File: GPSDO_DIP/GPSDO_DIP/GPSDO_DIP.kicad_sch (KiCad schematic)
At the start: 86 parts, among them IC2 74HC14, K1 Conn_01x04, K2 Conn_Coaxial, K3 Conn_01x02, K4 Jumper_3_Open, K5 Conn_01x02, K9 Conn_Coaxial, U1 Pico, U10 U1, U11 74HC14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

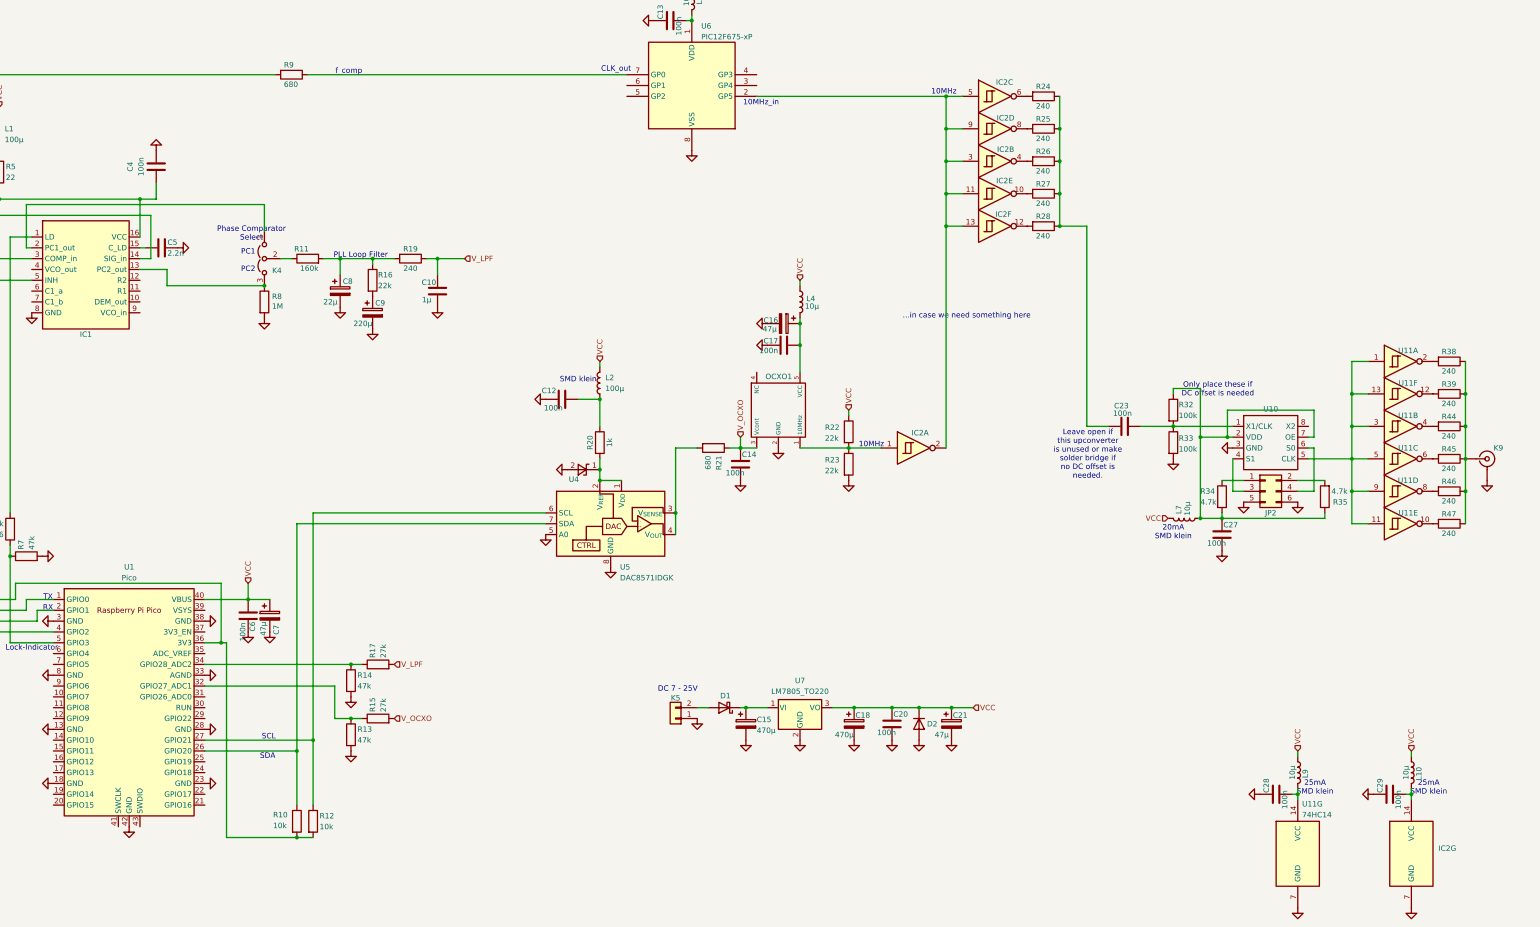
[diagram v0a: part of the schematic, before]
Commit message: added mounting holes & 10MHz SMA-port, cleaned up labels a bit
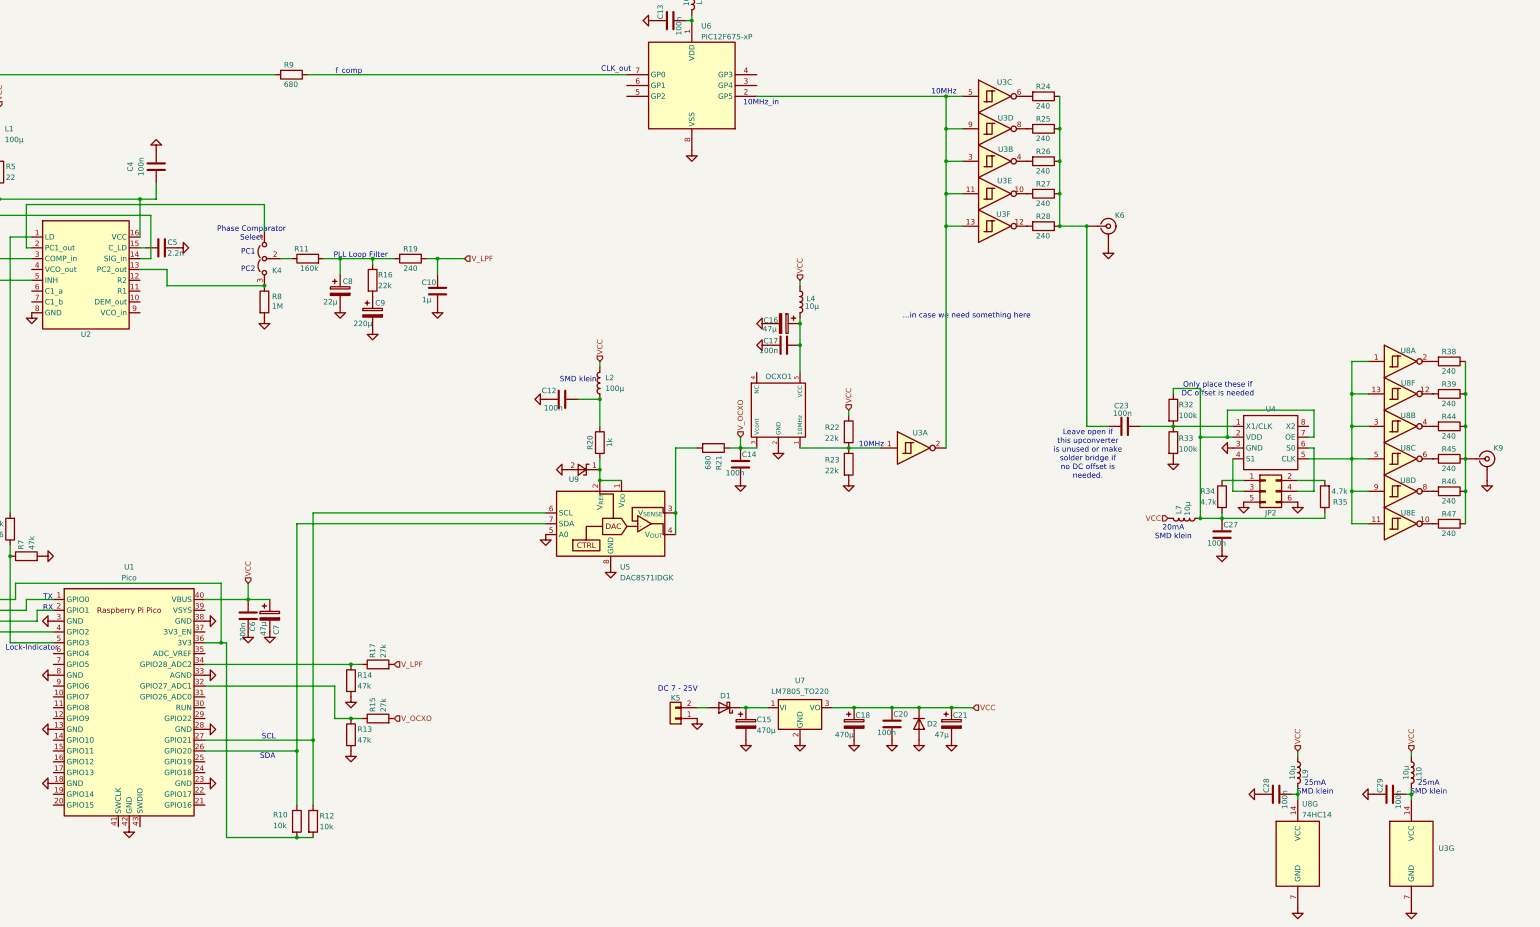
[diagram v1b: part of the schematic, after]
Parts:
- added K6: Conn_Coaxial, Connector_Coaxial:SMA_Molex_73251-1153_EdgeMount_Horizontal, symbol Connector:Conn_Coaxial
- renumbered IC1 to U2, IC2 to U3, U10 to U4, U11 to U8, U4 to U9
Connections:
- net GND: now also K6.2 (Ext)
- net at C23.2, R24.1, R25.1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: now also K6.1 (In)
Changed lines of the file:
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@@
 	)
 	(junction
+		(at 307.34 87.63)
+		(diameter 0)
+		(color 0 0 0 0)
+	)
+	(junction
 		(at 383.54 220.98)
 		(diameter 0)
@@
 		(on_board yes)
 		(dnp no)
-		(property "Reference" "IC2"
+		(property "Reference" "U3"
 			(at 288.036 53.848 0)
 			(effects
@@
 			(project "GPSDO_DIP"
 				(path "/39e4adc2-ce33-4fe2-95cd-1c444a71fa67"
-					(reference "IC2")
+					(reference "U3")
 					(unit 3)
 				)
@@
 	)
 	(symbol
+		(lib_id "power:GND")
+		(at 312.42 92.71 0)
+		(unit 1)
+		(exclude_from_sim no)
+		(in_bom yes)
+		(on_board yes)
+		(dnp no)
+		(fields_autoplaced yes)
+		(property "Reference" "#PWR022"
+			(at 312.42 99.06 0)
+			(effects
+				(font
+					(size 1.27 1.27)
+				)
+				(hide yes)
+			)
+		)
+		(property "Value" "GND"
+			(at 312.42 97.79 0)
+			(effects
+				(font
+					(size 1.27 1.27)
+				)
+				(hide yes)
+			)
+		)
+		(property "Footprint" ""
+			(at 312.42 92.71 0)
+			(effects
+				(font
+					(size 1.27 1.27)
+				)
+				(hide yes)
+			)
+		)
+		(property "Datasheet" ""
+			(at 312.42 92.71 0)
+			(effects
+				(font
+					(size 1.27 1.27)
+				)
+				(hide yes)
+			)
+		)
+		(property "Description" "Power symbol creates a global label with name \"GND\" , ground"
+			(at 312.42 92.71 0)
+			(effects
+				(font
+					(size 1.27 1.27)
+				)
+				(hide yes)
+			)
+		)
+		(pin "1"
+		)
+		(instances
+			(project "GPSDO_DIP"
+				(path "/39e4adc2-ce33-4fe2-95cd-1c444a71fa67"
+					(reference "#PWR022")
+					(unit 1)
+				)
+			)
+		)
+	)
+	(symbol
 		(lib_id "Device:R")
 		(at 140.97 190.5 90)
@@
 		(dnp no)
 		(fields_autoplaced yes)
-		(property "Reference" "IC2"
+		(property "Reference" "U3"
 			(at 389.89 233.6799 0)
 			(effects
@@
 			(project "GPSDO_DIP"
 				(path "/39e4adc2-ce33-4fe2-95cd-1c444a71fa67"
-					(reference "IC2")
+					(reference "U3")
 					(unit 7)
 				)
@@
 		(on_board yes)
 		(dnp no)
-		(property "Reference" "IC2"
+		(property "Reference" "U3"
 			(at 288.29 62.23 0)
 			(effects
@@
 			(project "GPSDO_DIP"
 				(path "/39e4adc2-ce33-4fe2-95cd-1c444a71fa67"
-					(reference "IC2")
+					(reference "U3")
 					(unit 4)
 				)
@@
 		(on_board yes)
 		(dnp no)
-		(property "Reference" "U11"
+		(property "Reference" "U8"
 			(at 382.778 147.32 0)
 			(effects
@@
 			(project "GPSDO_DIP"
 				(path "/39e4adc2-ce33-4fe2-95cd-1c444a71fa67"
-					(reference "U11")
+					(reference "U8")
 					(unit 4)
 				)
@@
 		(on_board yes)
 		(dnp no)
-		(property "Reference" "U11"
+		(property "Reference" "U8"
 			(at 382.778 154.94 0)
 			(effects
@@
 			(project "GPSDO_DIP"
 				(path "/39e4adc2-ce33-4fe2-95cd-1c444a71fa67"
-					(reference "U11")
+					(reference "U8")
 					(unit 5)
 				)
@@
 		(on_board yes)
 		(dnp no)
-		(property "Reference" "IC2"
+		(property "Reference" "U3"
 			(at 288.036 76.962 0)
 			(effects
@@
 			(project "GPSDO_DIP"
 				(path "/39e4adc2-ce33-4fe2-95cd-1c444a71fa67"
-					(reference "IC2")
+					(reference "U3")
 					(unit 5)
 				)
@@
 		(on_board yes)
 		(dnp no)
-		(property "Reference" "U11"
+		(property "Reference" "U8"
 			(at 357.886 223.266 0)
 			(effects
@@
 			(project "GPSDO_DIP"
 				(path "/39e4adc2-ce33-4fe2-95cd-1c444a71fa67"
-					(reference "U11")
+					(reference "U8")
 					(unit 7)
 				)
@@
 		(on_board yes)
 		(dnp no)
-		(property "Reference" "IC1"
+		(property "Reference" "U2"
 			(at 72.39 113.03 0)
 			(effects
@@
 			(project "GPSDO_DIP"
 				(path "/39e4adc2-ce33-4fe2-95cd-1c444a71fa67"
-					(reference "IC1")
+					(reference "U2")
 					(unit 1)
 				)
@@
 		(on_board yes)
 		(dnp no)
-		(property "Reference" "IC2"
+		(property "Reference" "U3"
 			(at 268.224 136.144 0)
 			(effects
@@
 			(project "GPSDO_DIP"
 				(path "/39e4adc2-ce33-4fe2-95cd-1c444a71fa67"
-					(reference "IC2")
+					(reference "U3")
 					(unit 1)
 				)
@@
 		(on_board yes)
 		(dnp no)
-		(property "Reference" "U11"
+		(property "Reference" "U8"
 			(at 382.778 132.08 0)
 			(effects
@@
 			(project "GPSDO_DIP"
 				(path "/39e4adc2-ce33-4fe2-95cd-1c444a71fa67"
-					(reference "U11")
+					(reference "U8")
 					(unit 2)
 				)
@@
 		(on_board yes)
 		(dnp no)
-		(property "Reference" "IC2"
+		(property "Reference" "U3"
 			(at 288.29 69.596 0)
 			(effects
@@
 			(project "GPSDO_DIP"
 				(path "/39e4adc2-ce33-4fe2-95cd-1c444a71fa67"
-					(reference "IC2")
+					(reference "U3")
 					(unit 2)
 				)
@@
 		(on_board yes)
 		(dnp no)
-		(property "Reference" "IC2"
+		(property "Reference" "U3"
 			(at 287.782 84.836 0)
 			(effects
@@
 			(project "GPSDO_DIP"
 				(path "/39e4adc2-ce33-4fe2-95cd-1c444a71fa67"
-					(reference "IC2")
+					(reference "U3")
 					(unit 6)
 				)
@@
 		(on_board yes)
 		(dnp no)
-		(property "Reference" "U11"
+		(property "Reference" "U8"
 			(at 382.778 139.7 0)
 			(effects
@@
 			(project "GPSDO_DIP"
 				(path "/39e4adc2-ce33-4fe2-95cd-1c444a71fa67"
-					(reference "U11")
+					(reference "U8")
 					(unit 3)
 				)
@@
 		(on_board yes)
 		(dnp no)
-		(property "Reference" "U10"
+		(property "Reference" "U4"
 			(at 350.52 130.556 0)
 			(effects
@@
 			(project "GPSDO_DIP"
 				(path "/39e4adc2-ce33-4fe2-95cd-1c444a71fa67"
-					(reference "U10")
+					(reference "U4")
 					(unit 1)
 				)
@@
 		(on_board yes)
 		(dnp no)
-		(property "Reference" "U11"
+		(property "Reference" "U8"
 			(at 382.778 116.84 0)
 			(effects
@@
 			(project "GPSDO_DIP"
 				(path "/39e4adc2-ce33-4fe2-95cd-1c444a71fa67"
-					(reference "U11")
+					(reference "U8")
 					(unit 1)
 				)
@@
 		(on_board yes)
 		(dnp no)
-		(property "Reference" "U11"
+		(property "Reference" "U8"
 			(at 382.778 124.46 0)
 			(effects
@@
 			(project "GPSDO_DIP"
 				(path "/39e4adc2-ce33-4fe2-95cd-1c444a71fa67"
-					(reference "U11")
+					(reference "U8")
 					(unit 6)
 				)
@@
 	)
 	(symbol
+		(lib_id "Connector:Conn_Coaxial")
+		(at 312.42 87.63 0)
+		(unit 1)
+		(exclude_from_sim no)
+		(in_bom yes)
+		(on_board yes)
+		(dnp no)
+		(property "Reference" "K6"
+			(at 313.944 85.09 0)
+			(effects
+				(font
+					(size 1.27 1.27)
+				)
+				(justify left)
+			)
+		)
+		(property "Value" "Conn_Coaxial"
+			(at 316.23 89.1931 0)
+			(effects
+				(font
+					(size 1.27 1.27)
+				)
+				(justify left)
+				(hide yes)
+			)
+		)
+		(property "Footprint" "Connector_Coaxial:SMA_Molex_73251-1153_EdgeMount_Horizontal"
+			(at 312.42 87.63 0)
+			(effects
+				(font
+					(size 1.27 1.27)
+				)
+				(hide yes)
+			)
+		)
+		(property "Datasheet" " ~"
+			(at 312.42 87.63 0)
+			(effects
+				(font
+					(size 1.27 1.27)
+				)
+				(hide yes)
+			)
+		)
+		(property "Description" "coaxial connector (BNC, SMA, SMB, SMC, Cinch/RCA, LEMO, ...)"
+			(at 312.42 87.63 0)
+			(effects
+				(font
+					(size 1.27 1.27)
+				)
+				(hide yes)
+			)
+		)
+		(pin "1"
+		)
+		(pin "2"
+		)
+		(instances
+			(project "GPSDO_DIP"
+				(path "/39e4adc2-ce33-4fe2-95cd-1c444a71fa67"
+					(reference "K6")
+					(unit 1)
+				)
+			)
+		)
+	)
+	(symbol
 		(lib_id "power:GND")
 		(at 356.87 247.65 0)
@@
 		(on_board yes)
 		(dnp no)
-		(property "Reference" "U4"
+		(property "Reference" "U9"
 			(at 186.944 147.066 0)
 			(effects
@@
 			(project "GPSDO_DIP"
 				(path "/39e4adc2-ce33-4fe2-95cd-1c444a71fa67"
-					(reference "U4")
+					(reference "U9")
 					(unit 1)
 				)
